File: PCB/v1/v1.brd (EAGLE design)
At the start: 55 x 39 mm, 63 parts, among them U2 AT24C512C-SHD-B

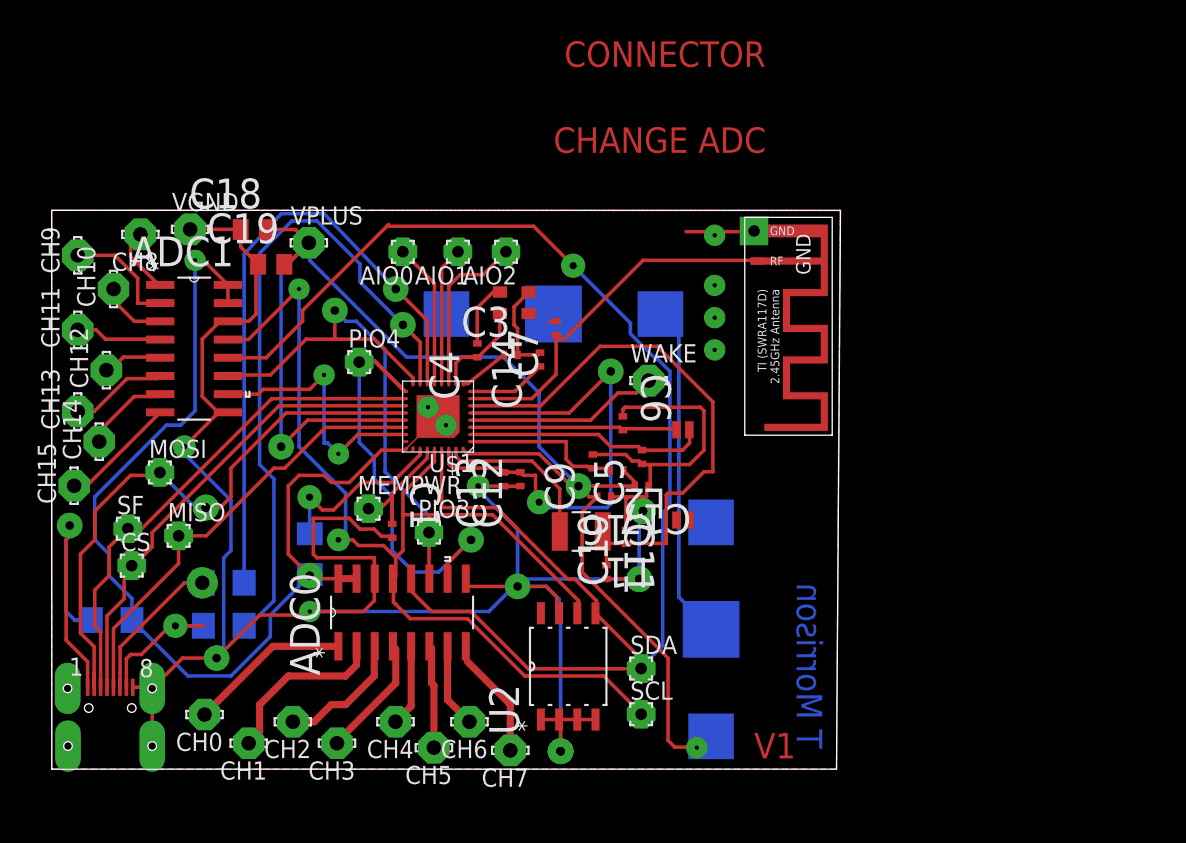
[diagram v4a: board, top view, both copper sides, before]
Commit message: added new chip, brought out solder mask. Need to check crystal pads and ground connections
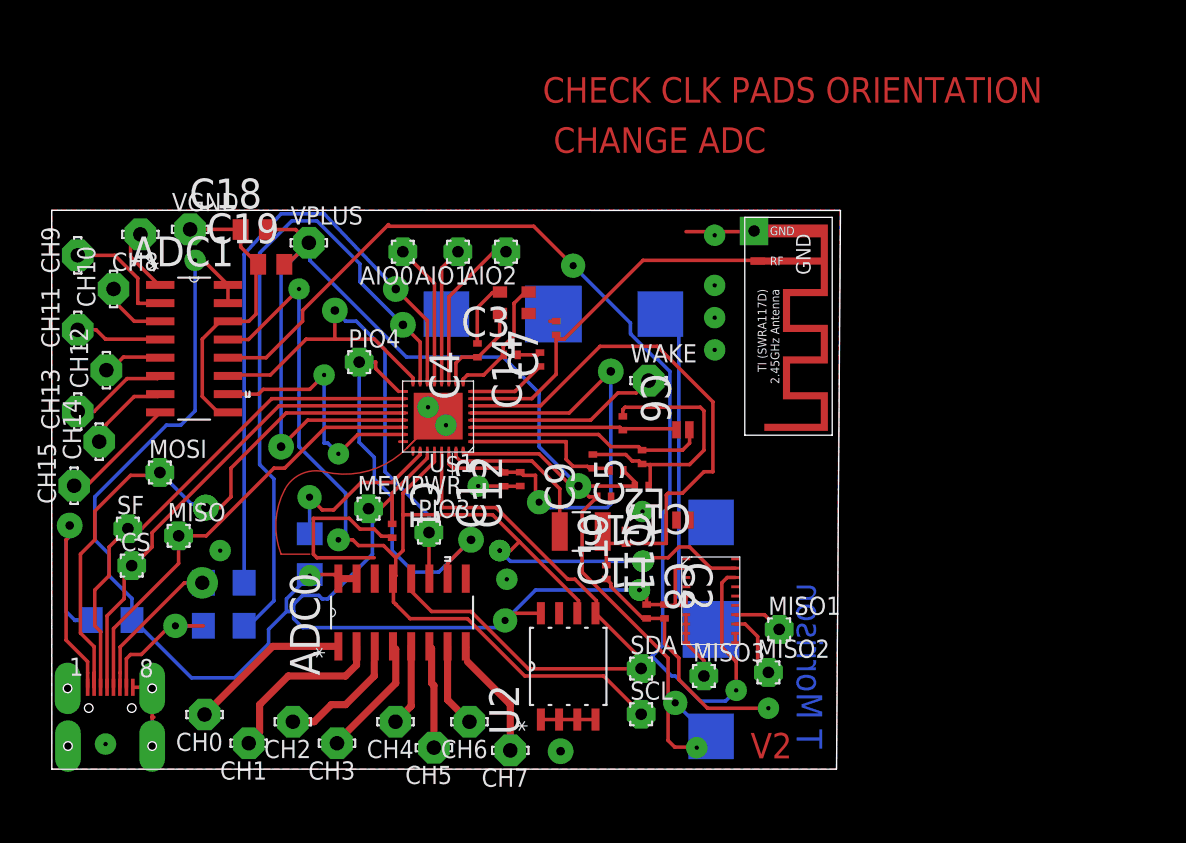
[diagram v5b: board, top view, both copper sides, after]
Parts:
- added C2: 1u, AVX_By_element14_Batch_1:CAPC1005X60N
- added C8: 0.1u, AVX_By_element14_Batch_1:CAPC1005X60N
- added MISO1, MISO2, MISO3: (no value), wirepad:1,6/0,8
- added U$7: AD7997, AD7997:AD7997
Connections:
- net N$28 renamed VDD_CORE
- removed net N$21: ADC0.13, ADC1.13, SCL.1, U$1.I2C_SCL, U2.6
- removed net N$22: ADC0.12, ADC1.12, SDA.1, U$1.I2C_SDA, U2.5
- removed net N$46: C1.1, MEMPWR.1, U$1.PIO[2]
- removed net VCC: U2.8
- new net N$86: MISO1.1, U$7.P$014
- new net N$87: MISO2.1, U$7.P$013
- new net N$88: MISO3.1, U$7.P$010, U$7.P$07
- new net N$90: U$7.P$011, U$7.P$012
- new net SCL: ADC0.13, ADC1.13, SCL.1, U$1.I2C_SCL, U$7.P$019, U2.6
- new net SDA: ADC0.12, ADC1.12, SDA.1, U$1.I2C_SDA, U$7.P$018, U2.5
- net GND: now also C2.2, C8.2, U$7.P$01, U$7.P$015, U$7.P$020, U$7.P$03, U$7.P$04
- net VDD: now also C1.1, C2.1, C8.1, MEMPWR.1, U$1.PIO[2], U$7.P$02, U$7.P$05, U$7.P$06, U2.8
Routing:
- net SDA: track 0.00 -> 120.3 mm, vias 0 -> 2
- net N$22: track 104.2 -> 0.00 mm
- net SCL: track 0.00 -> 97.6 mm, vias 0 -> 4
- net N$21: track 78.5 -> 0.00 mm, vias 2 -> 1
- net GND: track 189.5 -> 112.2 mm, vias 12 -> 11
- net VDD: track 73.1 -> 111.6 mm, vias 2 -> 4
- net N$46: track 8.20 -> 0.00 mm
- net N$85: track 0.00 -> 5.12 mm
- net N$88: track 0.00 -> 4.79 mm
- net N$80: track 4.77 -> 0.00 mm
- net N$87: track 0.00 -> 4.72 mm
- net N$25: track 32.6 -> 28.4 mm
- net N$34: track 101.2 -> 105.2 mm, vias 2 -> 3
- net N$86: track 0.00 -> 3.47 mm
- net N$90: track 0.00 -> 0.65 mm
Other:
- board text added: "CHECK CLK PADS ORIENTATION"
- board text added: "V2"
- board text removed: "CONNECTOR"
- board text removed: "V1"

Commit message: need to check over
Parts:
- moved C10 1.05 mm to (39.7, 17.2)
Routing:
- net GND: track 112.2 -> 124.5 mm, vias 11 -> 14
- net N$39: track 40.0 -> 38.7 mm
- net SCL: track 97.6 -> 98.4 mm
- net N$25: track 28.4 -> 27.8 mm

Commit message: do a once over, then fab
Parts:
- added C15: 1u, AVX_By_element14_Batch_1:CAPC1005X60N
- added C20: 0.1u, AVX_By_element14_Batch_1:CAPC1005X60N
- added R1, R2: 10K, rcl:R0402
- moved PIO3 0.50 mm to (25.8, 16.5)
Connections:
- net GND: now also C15.2
- net SCL: now also R1.1
- net SDA: now also R2.1
- net VDD: now also C15.1, C20.1, R1.2, R2.2
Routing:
- net VDD: track 111.6 -> 141.1 mm
- net GND: track 124.5 -> 151.7 mm, vias 14 -> 15
- net SCL: track 98.4 -> 102.2 mm
- net SDA: track 120.4 -> 124.1 mm
- net N$25: track 27.8 -> 27.2 mm
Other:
- board text removed: "CHANGE ADC"
- board text removed: "CHECK CLK PADS ORIENTATION"
